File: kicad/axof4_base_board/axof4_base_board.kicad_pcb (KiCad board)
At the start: 2 copper layers, 52 parts, among them J1 CLK_OUT, U1 CODECODER-WM8731SEDS_V(SSOP28), U2 23LC1024-I_SN, Y1 12.288MHz

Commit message: work on kicad project
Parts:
- added J2: PJ-102A, digikey-footprints:Barrel_Jack_5.5mmODx2.1mmID_PJ-102A, F.Cu at (263.5, 158.1)
- added U4: LM1117MPX-3_3_NOPB, digikey-footprints:SOT-223, F.Cu at (272.8, 151.6)
- added U5: LM1117MPX-3_3_NOPB, digikey-footprints:SOT-223, F.Cu at (280.8, 151.6)
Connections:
- C1 pad 2: GNDA -> GND
- C10 pad 2: GNDA -> GND
- C11 pad 2: GNDA -> GND
- C12 pad 2: GNDA -> GND
- C2 pad 2: GNDA -> GND
- C20 pad 2: GNDA -> GND
- C21 pad 2: GNDA -> GND
- C22 pad 2: GNDA -> GND
- C9 pad 2: GNDA -> GND
- JB1 pad P1_3: Net-(JB1-PadP1_3) -> +3V3
- JB1 pad P1_4: Net-(JB1-PadP1_3) -> +3V3
- JB1 pad P2_22: Net-(JB1-PadP1_3) -> +3V3
- R17 pad 2: GNDA -> GND
- R18 pad 2: GNDA -> GND
- R19 pad 2: GNDA -> GND
- R3 pad 2: GNDA -> GND
- R4 pad 2: GNDA -> GND
- R5 pad 2: GNDA -> GND
- R6 pad 2: GNDA -> GND
- U1 pad 11: GNDA -> GND
- U1 pad 15: GNDA -> GND

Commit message: cleanup, dedicated PCB WIP
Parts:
- added C24: 10p, Capacitor_SMD:C_1206_3216Metric_Pad1.42x1.75mm_HandSolder, F.Cu at (301.3, 32.5)
- added C25: 100u, Capacitor_SMD:CP_Elec_4x5.4, F.Cu at (294.4, 32.4)
- added C26: 100u, Capacitor_SMD:CP_Elec_4x5.4, F.Cu at (286.7, 38.4)
- added C27: 1u, Capacitor_SMD:CP_Elec_4x5.4, F.Cu at (298.8, 26.6)
- added C28: 10u, Capacitor_SMD:CP_Elec_4x5.4, F.Cu at (277.1, 44.2)
- added C29: 10u, Capacitor_SMD:CP_Elec_4x5.4, F.Cu at (286.7, 32.5)
- added C30: 10u, Capacitor_SMD:CP_Elec_4x5.4, F.Cu at (278.9, 38.4)
- added C31: 100n, Capacitor_SMD:C_1206_3216Metric_Pad1.42x1.75mm_HandSolder, F.Cu at (264.7, 47.2)
- added C32: 100n, Capacitor_SMD:C_1206_3216Metric_Pad1.42x1.75mm_HandSolder, F.Cu at (282.5, 48.8)
- added C33: 100u, Capacitor_SMD:C_1206_3216Metric_Pad1.42x1.75mm_HandSolder, F.Cu at (291.7, 43.0)
- added C34: 10u, Capacitor_SMD:CP_Elec_4x5.4, F.Cu at (278.9, 32.5)
- added C35: 220u, Capacitor_SMD:CP_Elec_4x5.4, F.Cu at (291.0, 26.6)
- added C36: 220u, Capacitor_SMD:CP_Elec_4x5.4, F.Cu at (284.9, 44.2)
- added C37: 100n, Capacitor_SMD:C_1206_3216Metric_Pad1.42x1.75mm_HandSolder, F.Cu at (276.6, 48.8)
- added C38: 100n, Capacitor_SMD:C_1206_3216Metric_Pad1.42x1.75mm_HandSolder, F.Cu at (293.5, 37.0)
- added C39: 100n, Capacitor_SMD:C_1206_3216Metric_Pad1.42x1.75mm_HandSolder, F.Cu at (152.3, 140.0)
- added C40: 10u, Capacitor_SMD:CP_Elec_4x5.4, F.Cu at (141.0, 147.3)
- added D1: 1N4001, Diode_THT:D_DO-41_SOD81_P10.16mm_Horizontal, F.Cu at (263.6, 25.8)
- added D2: 1N4148, Diode_THT:D_DO-35_SOD27_P7.62mm_Horizontal, F.Cu at (140.1, 140.1)
- added J3: power_sw, Connector_PinHeader_2.54mm:PinHeader_1x02_P2.54mm_Vertical, F.Cu at (305.0, 26.0)
- added J4: MIDI_IN, Connector_PinHeader_2.54mm:PinHeader_1x03_P2.54mm_Vertical, F.Cu at (156.2, 128.3)
- added J5: MIDI_OUT, Connector_PinHeader_2.54mm:PinHeader_1x03_P2.54mm_Vertical, F.Cu at (151.7, 128.9)
- added J6: SD_Card, Connector_Card:SD_TE_2041021, F.Cu at (43.2, 95.2)
- added R25: 4.7, Resistor_SMD:R_1206_3216Metric_Pad1.42x1.75mm_HandSolder, F.Cu at (270.6, 48.8)
- added R26: 220, Resistor_SMD:R_1206_3216Metric_Pad1.42x1.75mm_HandSolder, F.Cu at (161.7, 128.3)
- added R27: 470, Resistor_SMD:R_1206_3216Metric_Pad1.42x1.75mm_HandSolder, F.Cu at (157.0, 135.5)
- added R28: 47, Resistor_SMD:R_1206_3216Metric_Pad1.42x1.75mm_HandSolder, F.Cu at (161.7, 131.6)
- added R29: 47, Resistor_SMD:R_1206_3216Metric_Pad1.42x1.75mm_HandSolder, F.Cu at (158.2, 138.8)
- added R30: 47k, Resistor_SMD:R_1206_3216Metric_Pad1.42x1.75mm_HandSolder, F.Cu at (140.1, 151.9)
- added R31: 47k, Resistor_SMD:R_1206_3216Metric_Pad1.42x1.75mm_HandSolder, F.Cu at (147.8, 146.0)
- added R32: 47k, Resistor_SMD:R_1206_3216Metric_Pad1.42x1.75mm_HandSolder, F.Cu at (146.0, 151.9)
- added R33: 47k, Resistor_SMD:R_1206_3216Metric_Pad1.42x1.75mm_HandSolder, F.Cu at (152.0, 149.3)
- added R34: 47k, Resistor_SMD:R_1206_3216Metric_Pad1.42x1.75mm_HandSolder, F.Cu at (152.0, 152.6)
- added U3: LT1054, Package_DIP:DIP-8_W7.62mm, F.Cu at (264.2, 30.5)
- added U6: L7805, Package_TO_SOT_THT:TO-220-3_Vertical, F.Cu at (264.9, 43.6)
- added U7: L7905, Package_TO_SOT_THT:TO-220-3_Vertical, F.Cu at (278.8, 27.6)
- added U8: 6N137, Package_DIP:DIP-8_W7.62mm, F.Cu at (140.2, 128.7)
- moved R21 163.1 mm to (153.0, 25.3)
- moved R23 160.3 mm to (159.0, 25.3)
- moved R8 142.3 mm to (111.3, 153.1)
- moved R7 142.0 mm to (99.4, 152.5)
- moved C19 138.0 mm to (96.5, 136.2)
- moved C18 137.9 mm to (84.8, 145.9)
- moved C5 135.5 mm to (92.6, 145.9)
- moved C9 135.3 mm to (100.3, 142.0)
- moved C17 134.1 mm to (107.2, 140.0)
- moved R13 134.0 mm to (119.1, 142.0)
- moved R14 134.0 mm to (119.1, 138.8)
- moved R20 130.1 mm to (117.3, 151.9)
- moved R11 130.1 mm to (111.3, 149.8)
- moved R16 128.3 mm to (125.0, 141.4)
- moved R19 128.3 mm to (125.0, 144.7)
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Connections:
- R21 pad 1: I2C_SCL -> I2C_SDA
- R23 pad 1: I2C_SDA -> I2C_SCL

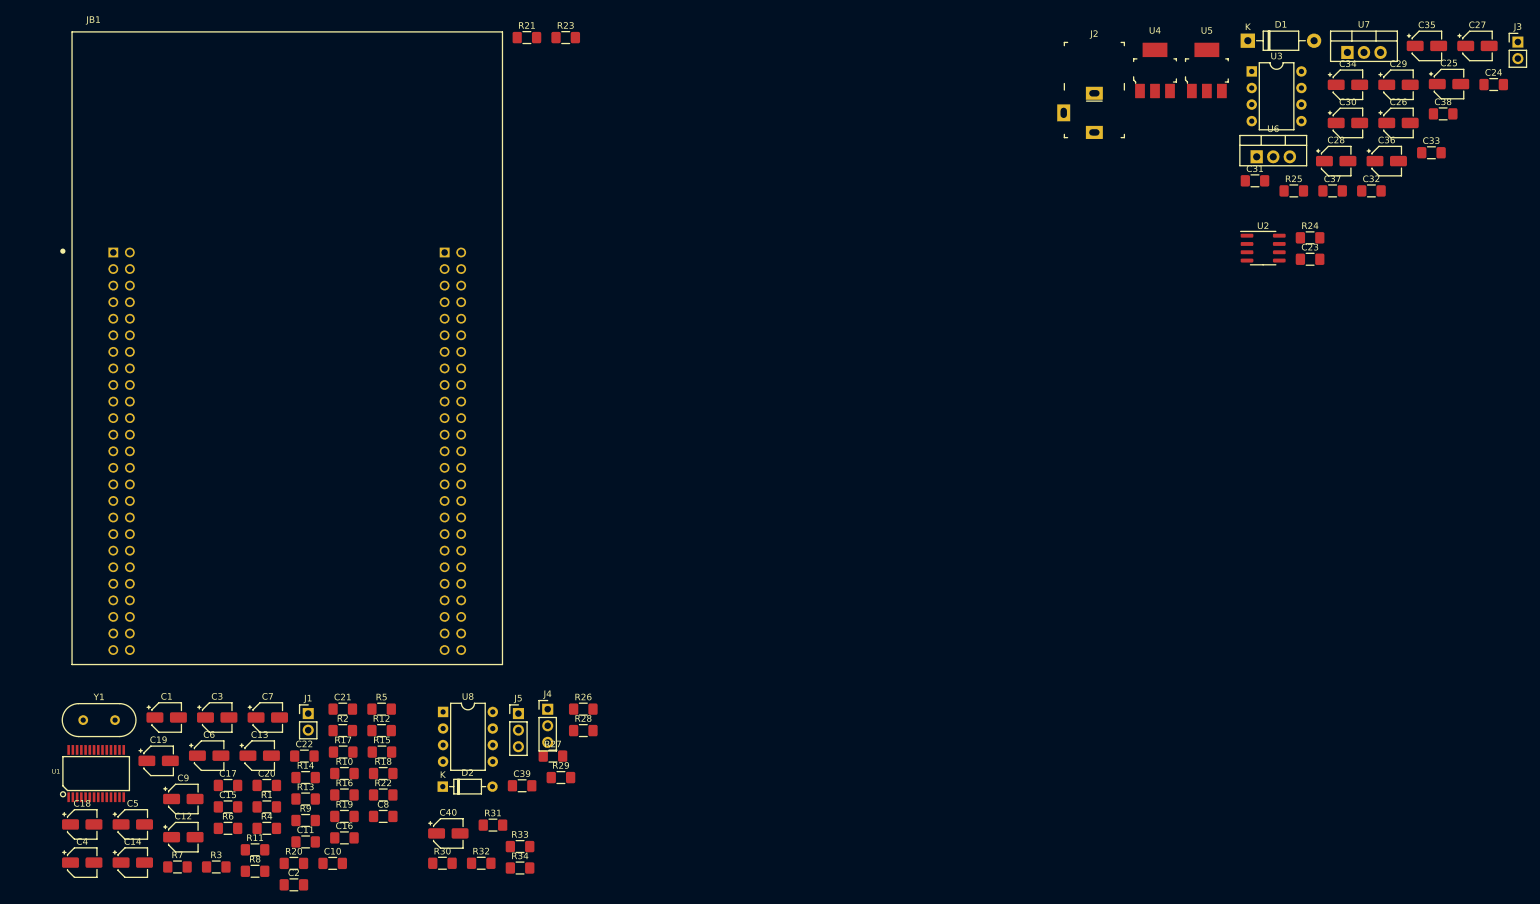
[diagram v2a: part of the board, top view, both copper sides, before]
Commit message: rollback kicad project to use STM32F4DISCOVERY
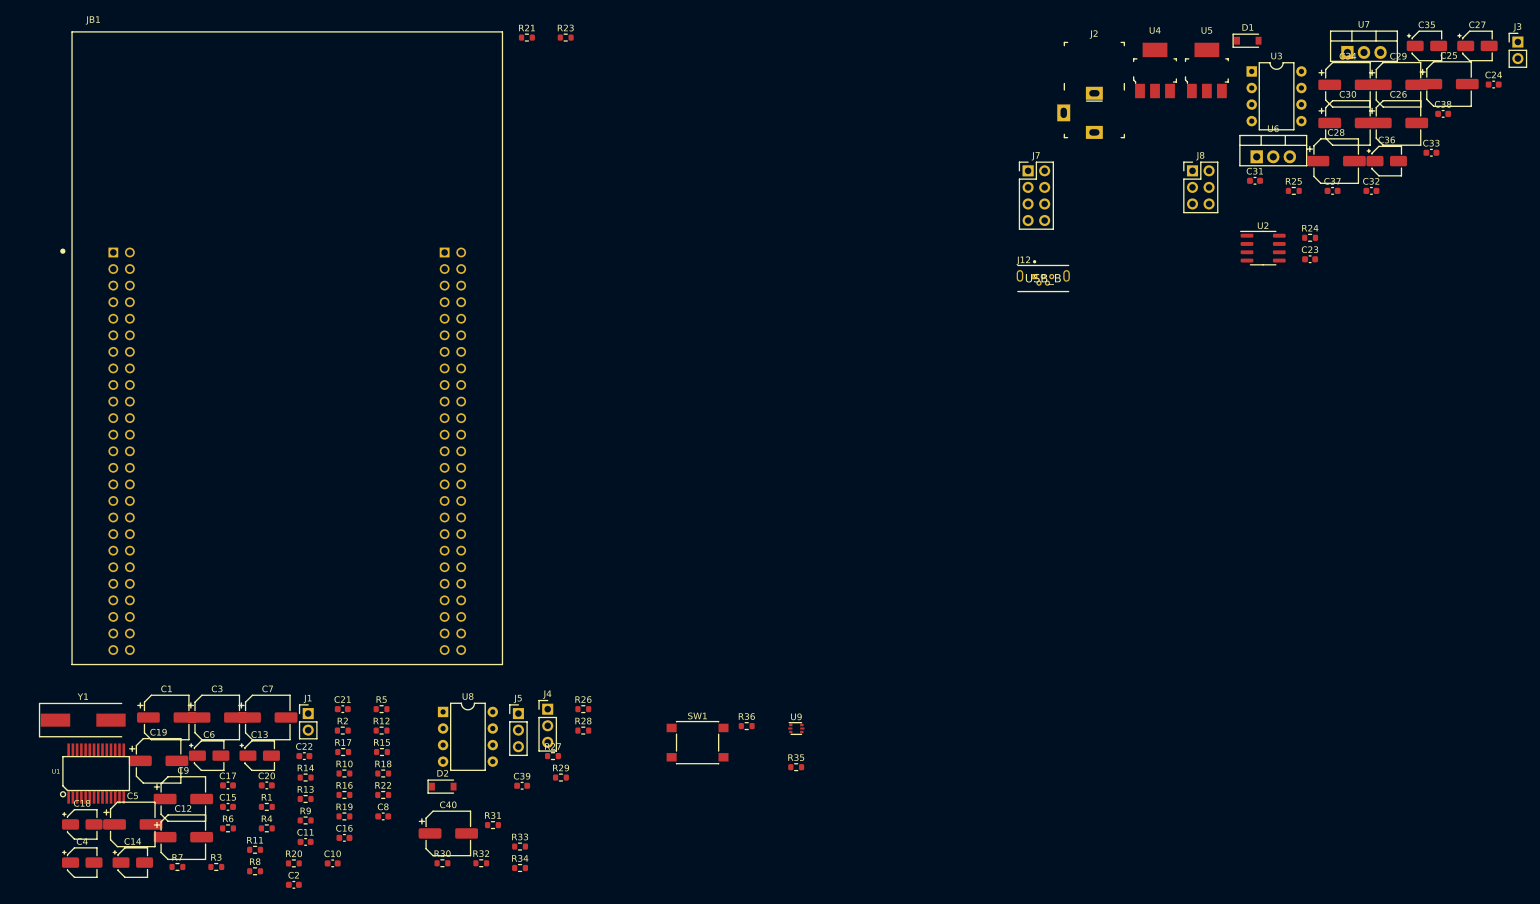
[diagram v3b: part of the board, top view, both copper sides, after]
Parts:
- added J12: USB_B, eec:GLOBAL_CONNECTOR_TECHNOLOGY-USB3145-30-1-A-0, F.Cu at (232.2, 62.2)
- added J7: I2C1_HEADER, Connector_PinHeader_2.54mm:PinHeader_2x04_P2.54mm_Vertical, F.Cu at (229.9, 45.7)
- added J8: SPI2_HEADER, Connector_PinHeader_2.54mm:PinHeader_2x03_P2.54mm_Vertical, F.Cu at (255.1, 45.7)
- added R35: 10k, Resistor_SMD:R_0603_1608Metric, F.Cu at (194.3, 137.2)
- added R36: 10k, Resistor_SMD:R_0603_1608Metric, F.Cu at (186.7, 130.9)
- added SW1: BOOT, Button_Switch_SMD:SW_Push_1P1T_NO_6x6mm_H9.5mm, F.Cu at (179.2, 133.4)
- added U9: USBLC6-2P6, Package_TO_SOT_SMD:SOT-666, F.Cu at (194.3, 131.2)
- C1, C12, C19, C25, C26, C28, C29, C3, C30, C34, C40, C5, C7, C9: footprint Capacitor_SMD:CP_Elec_4x5.4 -> Capacitor_SMD:CP_Elec_6.3x5.3
- C10, C11, C15, C16, C17, C2, C20, C21, C22, C23, C24, C31, C32, C33, C37, C38, C39, C8: footprint Capacitor_SMD:C_1206_3216Metric_Pad1.42x1.75mm_HandSolder -> Capacitor_SMD:C_0603_1608Metric
- D1: footprint Diode_THT:D_DO-41_SOD81_P10.16mm_Horizontal -> Diode_SMD:D_SOD-123
- D2: footprint Diode_THT:D_DO-35_SOD27_P7.62mm_Horizontal -> Diode_SMD:D_SOD-123
- R1, R10, R11, R12, R13, R14, R15, R16, R17, R18, R19, R2, R20, R21, R22, R23, R24, R25, R26, R27, R28, R29, R3, R30, R31, R32, R33, R34, R4, R5, R6, R7, R8, R9: footprint Resistor_SMD:R_1206_3216Metric_Pad1.42x1.75mm_HandSolder -> Resistor_SMD:R_0603_1608Metric
- Y1: footprint Crystal:Crystal_HC49-U_Vertical -> Crystal:Crystal_SMD_HC49-SD
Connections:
- net I2C_SCL renamed WM8731_SCL
- net I2C_SDA renamed WM8731_SDA
- net SPIRAM_MOSI-VGA_PIXEL renamed SPIRAM_MOSI
- J2 pad 3: Net-(J2-Pad3) -> (no net)
- J4 pad 2: Net-(J4-Pad2) -> (no net)
- J6 pad 10: Net-(J6-Pad10) -> (no net)
- J6 pad 11: Net-(J6-Pad11) -> (no net)
- JB1 pad P1_10: Net-(JB1-PadP1_10) -> (no net)
- JB1 pad P1_11: VGA_VSYNC -> (no net)
- JB1 pad P1_12: Net-(JB1-PadP1_12) -> (no net)
- JB1 pad P1_13: Net-(JB1-PadP1_13) -> (no net)
- JB1 pad P1_14: Net-(JB1-PadP1_14) -> (no net)
- JB1 pad P1_15: DAC2 -> (no net)
- JB1 pad P1_16: DAC1 -> (no net)
- JB1 pad P1_17: Net-(JB1-PadP1_17) -> (no net)
- JB1 pad P1_18: Net-(JB1-PadP1_18) -> (no net)
- JB1 pad P1_19: Net-(JB1-PadP1_19) -> (no net)
- JB1 pad P1_20: Net-(JB1-PadP1_20) -> (no net)
- JB1 pad P1_21: Net-(JB1-PadP1_21) -> (no net)
- JB1 pad P1_22: Net-(JB1-PadP1_22) -> SPI2_SOFT_NSS
- JB1 pad P1_24: Net-(JB1-PadP1_24) -> (no net)
- JB1 pad P1_25: Net-(JB1-PadP1_25) -> (no net)
- JB1 pad P1_26: Net-(JB1-PadP1_26) -> (no net)
- JB1 pad P1_27: Net-(JB1-PadP1_27) -> (no net)
- JB1 pad P1_28: Net-(JB1-PadP1_28) -> (no net)
- JB1 pad P1_29: Net-(JB1-PadP1_29) -> (no net)
- JB1 pad P1_30: Net-(JB1-PadP1_30) -> (no net)
- JB1 pad P1_31: Net-(JB1-PadP1_31) -> (no net)
- JB1 pad P1_32: Net-(JB1-PadP1_32) -> (no net)
- JB1 pad P1_33: Net-(JB1-PadP1_33) -> (no net)
- JB1 pad P1_40: Net-(JB1-PadP1_40) -> (no net)
- JB1 pad P1_41: Net-(JB1-PadP1_41) -> (no net)
- JB1 pad P1_42: Net-(JB1-PadP1_42) -> (no net)
- JB1 pad P1_43: Net-(JB1-PadP1_43) -> (no net)
- JB1 pad P1_44: Net-(JB1-PadP1_44) -> (no net)
- JB1 pad P1_45: Net-(JB1-PadP1_45) -> (no net)
- JB1 pad P1_46: Net-(JB1-PadP1_46) -> (no net)
- JB1 pad P1_47: Net-(JB1-PadP1_47) -> (no net)
- JB1 pad P1_6: Net-(JB1-PadP1_6) -> (no net)
- JB1 pad P1_7: Net-(JB1-PadP1_7) -> (no net)
- JB1 pad P1_8: Net-(JB1-PadP1_8) -> (no net)
- JB1 pad P1_9: Net-(JB1-PadP1_9) -> (no net)
- JB1 pad P2_10: Net-(JB1-PadP2_10) -> (no net)
- JB1 pad P2_11: Net-(JB1-PadP2_11) -> (no net)
- JB1 pad P2_12: Net-(JB1-PadP2_12) -> (no net)
- JB1 pad P2_13: Net-(JB1-PadP2_13) -> (no net)
- JB1 pad P2_14: Net-(JB1-PadP2_14) -> (no net)
- JB1 pad P2_15: Net-(JB1-PadP2_15) -> (no net)
- JB1 pad P2_16: Net-(JB1-PadP2_16) -> (no net)
- JB1 pad P2_17: Net-(JB1-PadP2_17) -> (no net)
- JB1 pad P2_18: Net-(JB1-PadP2_18) -> (no net)
- JB1 pad P2_19: Net-(JB1-PadP2_19) -> (no net)
- JB1 pad P2_20: Net-(JB1-PadP2_20) -> I2C1_SDA
- JB1 pad P2_23: Net-(JB1-PadP2_23) -> I2C1_SCL
- JB1 pad P2_24: Net-(JB1-PadP2_24) -> (no net)
- JB1 pad P2_27: Net-(JB1-PadP2_27) -> (no net)
- JB1 pad P2_29: Net-(JB1-PadP2_29) -> (no net)
- JB1 pad P2_30: Net-(JB1-PadP2_30) -> (no net)
- JB1 pad P2_31: Net-(JB1-PadP2_31) -> (no net)
- JB1 pad P2_32: Net-(JB1-PadP2_32) -> (no net)
- JB1 pad P2_33: Net-(JB1-PadP2_33) -> (no net)
- JB1 pad P2_36: Net-(JB1-PadP2_36) -> (no net)
- JB1 pad P2_39: Net-(JB1-PadP2_39) -> (no net)
- JB1 pad P2_41: Net-(JB1-PadP2_41) -> (no net)
- JB1 pad P2_42: Net-(JB1-PadP2_42) -> (no net)
- JB1 pad P2_43: VGA_HSYNC -> (no net)
- JB1 pad P2_44: Net-(JB1-PadP2_44) -> (no net)
- JB1 pad P2_48: Net-(JB1-PadP2_48) -> (no net)
- JB1 pad P2_7: Net-(JB1-PadP2_7) -> (no net)
- JB1 pad P2_8: Net-(JB1-PadP2_8) -> (no net)
- JB1 pad P2_9: Net-(JB1-PadP2_9) -> (no net)
- R1 pad 2: ROUT -> (no net)
- R2 pad 2: LOUT -> (no net)
- R20 pad 1: LLINEIN -> (no net)
- R22 pad 1: RLINEIN -> (no net)
- R28 pad 1: MIDI_TX -> (no net)
- U3 pad 1: Net-(U3-Pad1) -> (no net)
- U3 pad 6: Net-(U3-Pad6) -> (no net)
- U8 pad 1: Net-(U8-Pad1) -> (no net)
- U8 pad 7: Net-(U8-Pad7) -> (no net)

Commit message: blender edits
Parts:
- added R37: 0, Resistor_SMD:R_0603_1608Metric, F.Cu at (130.5, 148.4)
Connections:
- R12 pad 1: I2S_MCLK -> Net-(R12-Pad1)
- U1 pad 25: I2S_MCLK -> Net-(R12-Pad1)
